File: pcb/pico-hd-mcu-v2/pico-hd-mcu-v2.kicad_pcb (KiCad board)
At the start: 2 copper layers, 87 x 57 mm, 29 parts

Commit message: updat pcb add drill holes
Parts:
- added ?: , , F.Cu at (103.7, 20.0)
- added ?: , , F.Cu at (24.0, 30.4)
- added ?: , , F.Cu at (80.0, 72.5)
- added ?: , , F.Cu at (80.0, 20.0)
- added ?: , , F.Cu at (43.9, 72.5)
- added REF**: Pin_D1.0mm_L10.0mm, Connector_Pin:Pin_D1.0mm_L10.0mm, F.Cu at (103.7, 72.5)
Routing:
- net GND: track 260.1 -> 271.3 mm
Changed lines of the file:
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@@
     )
+  )
+  (footprint "" (layer "F.Cu")
+    (at 103.7 20)
+    (fp_text reference "" (at 0 0) (layer "F.SilkS")
+        (effects (font (size 1.27 1.27) (thickness 0.15)))
+    )
+    (fp_text value "" (at 0 0) (layer "F.SilkS")
+        (effects (font (size 1.27 1.27) (thickness 0.15)))
+    )
+    (pad "1" thru_hole circle (at -0.11 0) (size 3 3) (drill 2) (layers "*.Cu" "*.Mask"))
   )
   (footprint "Connector_PinHeader_2.54mm:Socker_PinHeader_1x05_P2.54mm_Dualside" (layer "F.Cu")
@@
       (net 30 "D_SPD"))
     (model "${KICAD6_3DMODEL_DIR}/Connector_PinHeader_2.54mm.3dshapes/PinHeader_1x02_P2.54mm_Vertical.wrl"
+      (offset (xyz 0 0 0))
+      (scale (xyz 1 1 1))
+      (rotate (xyz 0 0 0))
+    )
+  )
+  (footprint "Connector_Pin:Pin_D1.0mm_L10.0mm" (layer "F.Cu")
+    (at 103.7 72.5)
+    (descr "solder Pin_ diameter 1.0mm, hole diameter 1.0mm (press fit), length 10.0mm")
+    (tags "solder Pin_ press fit")
+    (attr through_hole)
+    (fp_text reference "REF**" (at 0 2.25) (layer "F.SilkS") hide
+        (effects (font (size 1 1) (thickness 0.15)))
+    )
+    (fp_text value "Pin_D1.0mm_L10.0mm" (at 0 -2.05) (layer "F.Fab") hide
+        (effects (font (size 1 1) (thickness 0.15)))
+    )
+    (fp_circle (center 0 0) (end 1.25 0.05)
+      (stroke (width 0.12) (type solid)) (fill none) (layer "F.SilkS"))
+    (fp_circle (center 0 0) (end 1.5 0)
+      (stroke (width 0.05) (type solid)) (fill none) (layer "F.CrtYd"))
+    (fp_circle (center 0 0) (end 0.5 0)
+      (stroke (width 0.12) (type solid)) (fill none) (layer "F.Fab"))
+    (fp_circle (center 0 0) (end 1 0)
+      (stroke (width 0.12) (type solid)) (fill none) (layer "F.Fab"))
+    (pad "1" thru_hole circle (at 0 0) (size 3 3) (drill 2) (layers "*.Cu" "*.Mask"))
+    (model "${KICAD6_3DMODEL_DIR}/Connector_Pin.3dshapes/Pin_D1.0mm_L10.0mm.wrl"
       (offset (xyz 0 0 0))
       (scale (xyz 1 1 1))
@@
       (net 1 "GND"))
   )
+  (footprint "" (layer "F.Cu")
+    (at 80 72.5)
+    (fp_text reference "" (at 0 0) (layer "F.SilkS")
+        (effects (font (size 1.27 1.27) (thickness 0.15)))
+    )
+    (fp_text value "" (at 0 0) (layer "F.SilkS")
+        (effects (font (size 1.27 1.27) (thickness 0.15)))
+    )
+    (pad "1" thru_hole circle (at 0 0) (size 3 3) (drill 2) (layers "*.Cu" "*.Mask"))
+  )
   (footprint "Resistor_THT:R_Axial_DIN0204_L3.6mm_D1.6mm_P2.54mm_Vertical" (layer "F.Cu")
     (at 51.76 31.49 90)
@@
     )
   )
+  (footprint "" (layer "F.Cu")
+    (at 80 20)
+    (fp_text reference "" (at 0 0) (layer "F.SilkS")
+        (effects (font (size 1.27 1.27) (thickness 0.15)))
+    )
+    (fp_text value "" (at 0 0) (layer "F.SilkS")
+        (effects (font (size 1.27 1.27) (thickness 0.15)))
+    )
+    (pad "1" thru_hole rect (at 0 0) (size 3 3) (drill 2) (layers "*.Cu" "*.Mask")
+      (net 1 "GND"))
+  )
   (footprint "Resistor_THT:R_Axial_DIN0204_L3.6mm_D1.6mm_P2.54mm_Vertical" (layer "F.Cu")
     (at 46.0775 41.8175)
@@
     (pad "V" thru_hole oval (at 9.13 -1.33 270) (size 1.7 1.7) (drill 1) (layers "*.Cu" "*.Mask")
       (net 7 "5V"))
+  )
+  (footprint "" (layer "F.Cu")
+    (at 43.87 72.54)
+    (fp_text reference "" (at 0 0) (layer "F.SilkS")
+        (effects (font (size 1.27 1.27) (thickness 0.15)))
+    )
+    (fp_text value "" (at 0 0) (layer "F.SilkS")
+        (effects (font (size 1.27 1.27) (thickness 0.15)))
+    )
+    (pad "1" thru_hole circle (at 0.13 -0.04) (size 3 3) (drill 2) (layers "*.Cu" "*.Mask"))
   )
   (footprint "" (layer "F.Cu")
@@
       (rotate (xyz 0 0 0))
     )
+  )
+  (footprint "" (layer "F.Cu")
+    (at 24 30.4)
+    (fp_text reference "" (at 0 0) (layer "F.SilkS")
+        (effects (font (size 1.27 1.27) (thickness 0.15)))
+    )
+    (fp_text value "" (at 0 0) (layer "F.SilkS")
+        (effects (font (size 1.27 1.27) (thickness 0.15)))
+    )
+    (pad "1" thru_hole circle (at 0 0) (size 3 3) (drill 2) (layers "*.Cu" "*.Mask"))
   )
   (footprint "denolk:switch_regulator_12v5v" (layer "B.Cu")
@@
     (effects (font (size 1 1) (thickness 0.15)) (justify mirror))
   )
-  (gr_text "denolk\nhd-mcu v0.2" (at 103.995 24.8825) (layer "B.SilkS")
+  (gr_text "denolk\nhd-mcu v0.2" (at 101.97 24.77) (layer "B.SilkS")
     (effects (font (size 1.5 1.5) (thickness 0.3) bold) (justify left bottom mirror))
   )
@@
   (segment (start 56.5425 26.2775) (end 74.3225 26.2775) (width 1) (layer "B.Cu") (net 1))
   (segment (start 45.92 33.04) (end 46.9575 34.0775) (width 1) (layer "B.Cu") (net 1))
+  (segment (start 74.3225 21.3075) (end 75.63 20) (width 1) (layer "B.Cu") (net 1))
   (segment (start 93.8 62.4325) (end 93.83 62.4025) (width 1) (layer "B.Cu") (net 1))
   (segment (start 50.4225 52.6225) (end 53.14 55.34) (width 1) (layer "B.Cu") (net 1))
@@
   (segment (start 46.0775 41.34) (end 47.935 39.4825) (width 1) (layer "B.Cu") (net 1))
   (segment (start 47.875 27.9925) (end 47.825 28.0425) (width 1) (layer "B.Cu") (net 1))
+  (segment (start 74.3225 26.2775) (end 74.3225 21.3075) (width 1) (layer "B.Cu") (net 1))
   (segment (start 47.825 28.0425) (end 47.855 28.0425) (width 1) (layer "B.Cu") (net 1))
   (segment (start 84.3275 62.4025) (end 78.0975 62.4025) (width 1) (layer "B.Cu") (net 1))
@@
   (segment (start 48.885 52.6225) (end 50.4225 52.6225) (width 1) (layer "B.Cu") (net 1))
   (segment (start 71 37.57) (end 71 26.2775) (width 1) (layer "B.Cu") (net 1))
+  (segment (start 75.63 20) (end 80 20) (width 1) (layer "B.Cu") (net 1))
   (segment (start 45.5025 41.8175) (end 43.54 43.78) (width 1) (layer "B.Cu") (net 1))
   (segment (start 53.14 55.34) (end 53.14 60.2) (width 1) (layer "B.Cu") (net 1))
@@
   (segment (start 84.7875 38.1125) (end 87.075 40.4) (width 1) (layer "B.Cu") (net 22))
   (segment (start 82.9175 38.1125) (end 84.7875 38.1125) (width 1) (layer "B.Cu") (net 22))
-  (segment (start 74.3225 66.9175) (end 76.2775 66.9175) (width 1) (layer "F.Cu") (net 23))
+  (segment (start 77.04 67.69) (end 88.92 67.69) (width 1) (layer "F.Cu") (net 23))
+  (segment (start 76.2675 66.9175) (end 77.04 67.69) (width 1) (layer "F.Cu") (net 23))
+  (segment (start 74.3225 66.9175) (end 76.2675 66.9175) (width 1) (layer "F.Cu") (net 23))
+  (segment (start 88.92 67.69) (end 91.315 70.085) (width 1) (layer "F.Cu") (net 23))
   (segment (start 91.315 70.085) (end 91.315 70.915) (width 1) (layer "F.Cu") (net 23))
-  (segment (start 78.02 68.66) (end 89.89 68.66) (width 1) (layer "F.Cu") (net 23))
-  (segment (start 89.89 68.66) (end 91.315 70.085) (width 1) (layer "F.Cu") (net 23))
-  (segment (start 76.2775 66.9175) (end 78.02 68.66) (width 1) (layer "F.Cu") (net 23))
-  (segment (start 74.3225 69.4575) (end 75.705 70.84) (width 1) (layer "F.Cu") (net 24))
-  (segment (start 75.705 70.84) (end 88.7 70.84) (width 1) (layer "F.Cu") (net 24))
-  (segment (start 88.7 70.84) (end 88.775 70.915) (width 1) (layer "F.Cu") (net 24))
+  (segment (start 87.35 69.49) (end 88.775 70.915) (width 1) (layer "F.Cu") (net 24))
+  (segment (start 74.3225 69.4575) (end 74.355 69.49) (width 1) (layer "F.Cu") (net 24))
+  (segment (start 74.355 69.49) (end 87.35 69.49) (width 1) (layer "F.Cu") (net 24))
   (segment (start 48.6175 44.4575) (end 52.2 44.4575) (width 1) (layer "B.Cu") (net 25))
   (segment (start 52.2 44.4575) (end 54.34 46.5975) (width 1) (layer "B.Cu") (net 25))

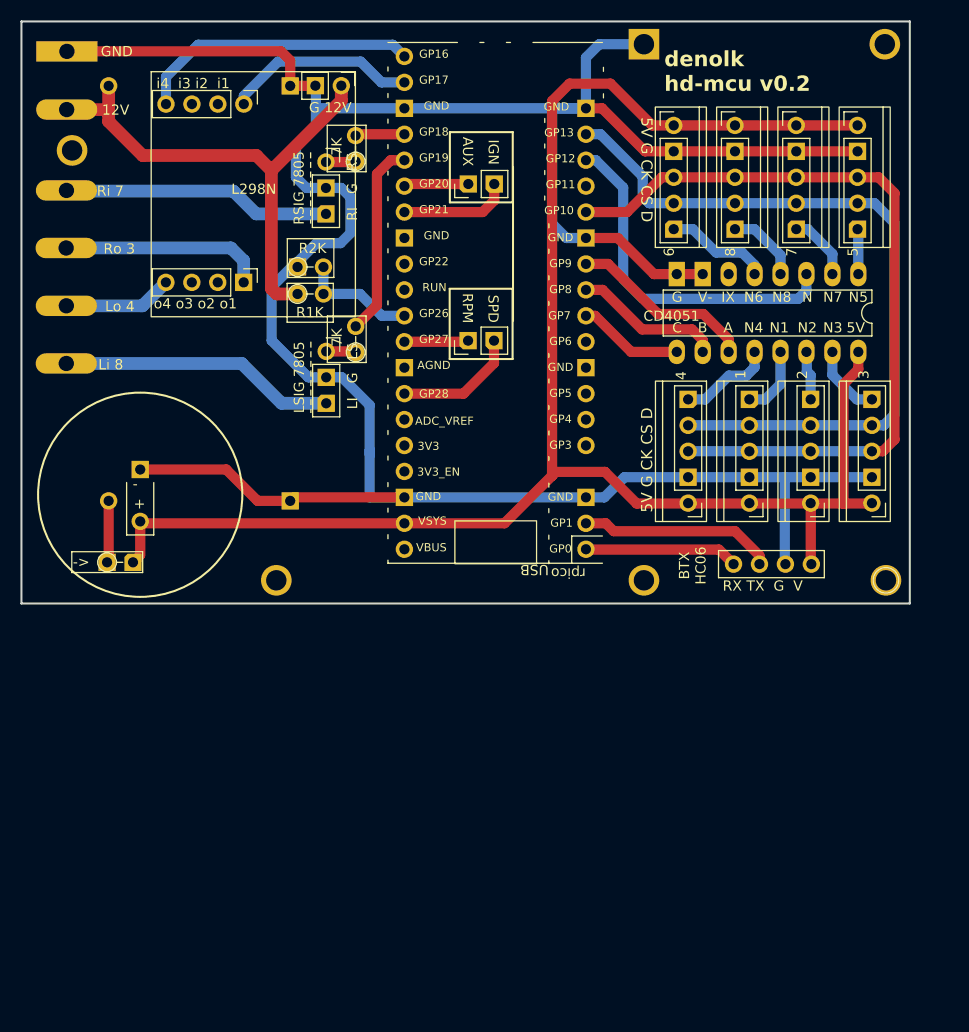
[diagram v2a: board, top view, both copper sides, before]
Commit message: add extension board for mux x4
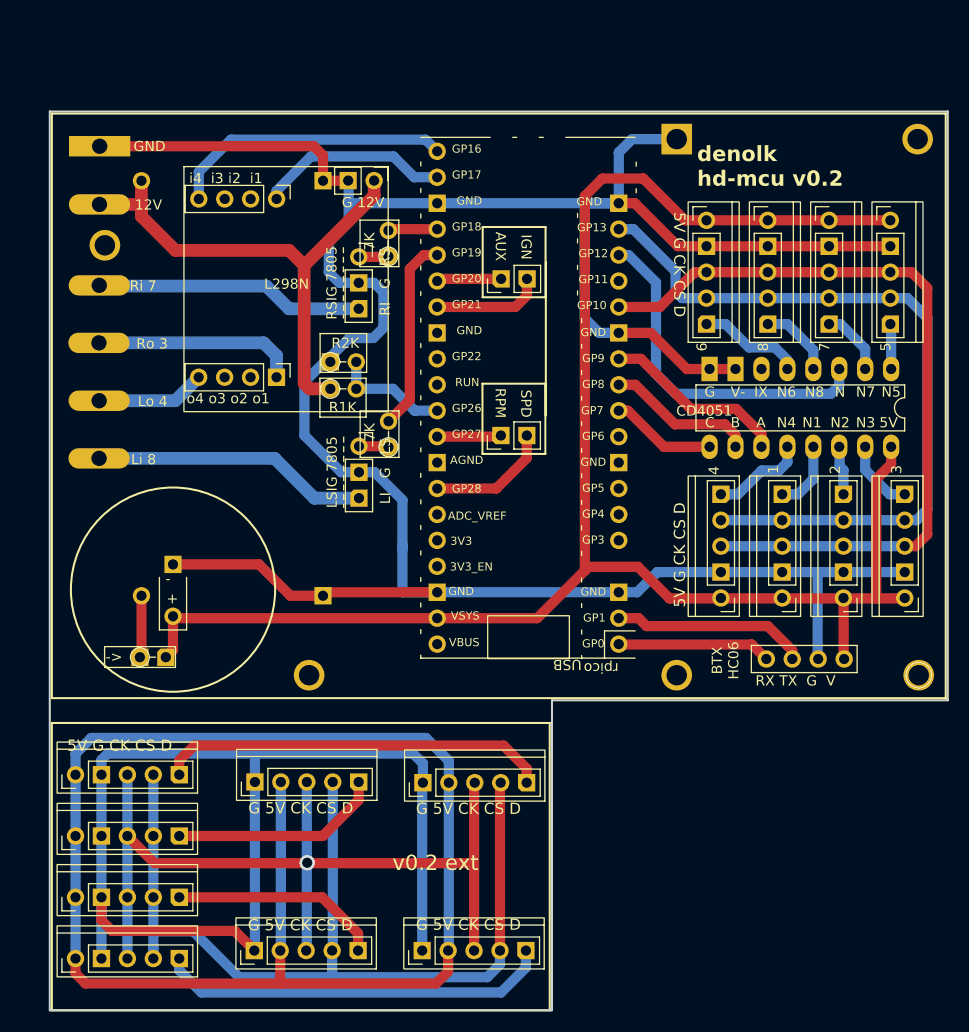
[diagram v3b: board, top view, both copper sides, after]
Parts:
- added 1: N1, Connector_PinHeader_2.54mm:Socker_PinHeader_1x05_P2.54mm_Dualside, F.Cu at (24.3, 97.5)
- added 1: N4, Connector_PinHeader_2.54mm:Socker_PinHeader_1x05_P2.54mm_Dualside, F.Cu at (41.9, 92.2)
- added 2: N4, Connector_PinHeader_2.54mm:Socker_PinHeader_1x05_P2.54mm_Dualside, F.Cu at (24.3, 103.5)
- added 2: N4, Connector_PinHeader_2.54mm:Socker_PinHeader_1x05_P2.54mm_Dualside, F.Cu at (41.8, 108.8)
- added 3: N4, Connector_PinHeader_2.54mm:Socker_PinHeader_1x05_P2.54mm_Dualside, F.Cu at (58.3, 108.8)
- added 3: N4, Connector_PinHeader_2.54mm:Socker_PinHeader_1x05_P2.54mm_Dualside, F.Cu at (24.3, 109.5)
- added 4: N4, Connector_PinHeader_2.54mm:Socker_PinHeader_1x05_P2.54mm_Dualside, F.Cu at (58.4, 92.3)
- added 4: N4, Connector_PinHeader_2.54mm:Socker_PinHeader_1x05_P2.54mm_Dualside, F.Cu at (24.3, 91.5)
- moved 1 9.83 mm to (93.5, 74.2)
- moved 2 9.83 mm to (99.5, 74.2)
- moved 3 9.83 mm to (105.5, 74.2)
- moved 4 9.83 mm to (87.5, 74.2)
- moved ? 9.83 mm to (83.2, 81.8)
- moved REF** 9.83 mm to (66.0, 43.0)
- moved -> 9.83 mm to (30.6, 80.0)
- moved ? 9.83 mm to (26.6, 49.2)
- moved ? 9.83 mm to (27.2, 39.7)
- moved ? 9.83 mm to (26.7, 35.7)
- moved REF** 9.83 mm to (33.9, 73.2)
- moved REF** 9.83 mm to (39.7, 58.2)
- moved ? 9.83 mm to (83.2, 29.3)
- moved 7K 9.83 mm to (55.0, 40.8)
- moved ? 9.83 mm to (26.7, 30.0)
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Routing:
- net x5V: track 0.00 -> 137.6 mm
- net xGND: track 0.00 -> 107.8 mm
- net xD_CS: track 0.00 -> 92.5 mm
- net xD_SCK: track 0.00 -> 86.1 mm, vias 0 -> 1
- net xMUX_S3: track 0.00 -> 38.7 mm
- net xMUX_S4: track 0.00 -> 38.3 mm
- net xMUX_S1: track 0.00 -> 20.8 mm
- net xMUX_S2: track 0.00 -> 20.7 mm
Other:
- board size 87 x 57 mm -> 87.9 x 88 mm
- board text added: "EXT"
- board text added: "G 5V CK CS D"
- board text added: "v0.2 ext"
